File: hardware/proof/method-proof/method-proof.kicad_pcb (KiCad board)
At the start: 4 copper layers, 40 x 30 mm, 21 parts, among them J1 5V_IN, J2 OUT, J3 PA1, U1 MCP1700T-3302E/TT, U2 MSPS003F4SPW20R

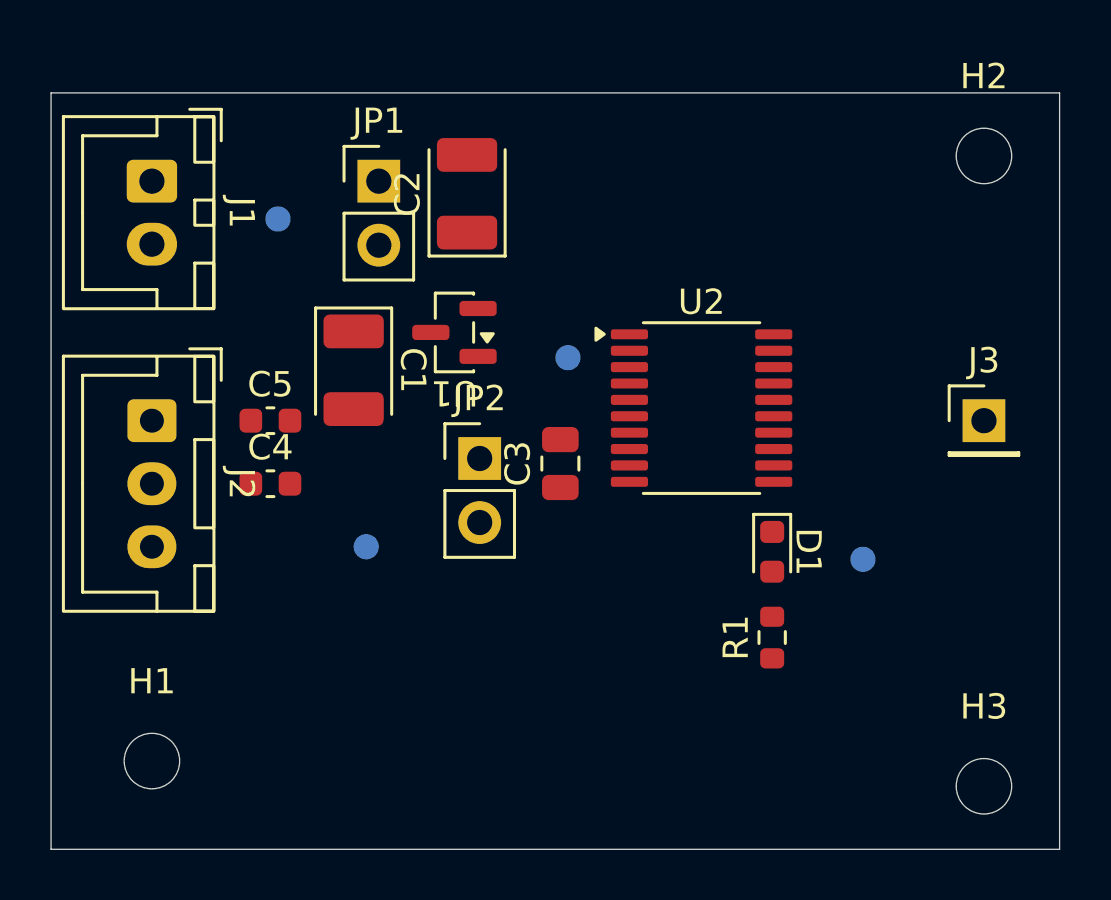
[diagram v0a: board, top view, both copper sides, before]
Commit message: hardware(method-proof): bring the footprints into step with their symbols and libraries: the symbols' fields, references on the fabrication layer, test points from the design's own library
Not for manufacture. Done with KiCad's scripting on the closed board, as the method
describes for what Konnect cannot do: each footprint carries its symbol's
description, datasheet and part fields, the mounting holes' BOM attribute follows
their symbols', the references move to the fabrication layers so no silkscreen
rule reaches them, and the four test points take the design's own footprint
library, whose copy Konnect can refresh from. The layout check reports no
violation but the unrouted connections.

Co-Authored-By: Claude Sonnet 5.5 <noreply@anthropic.com>
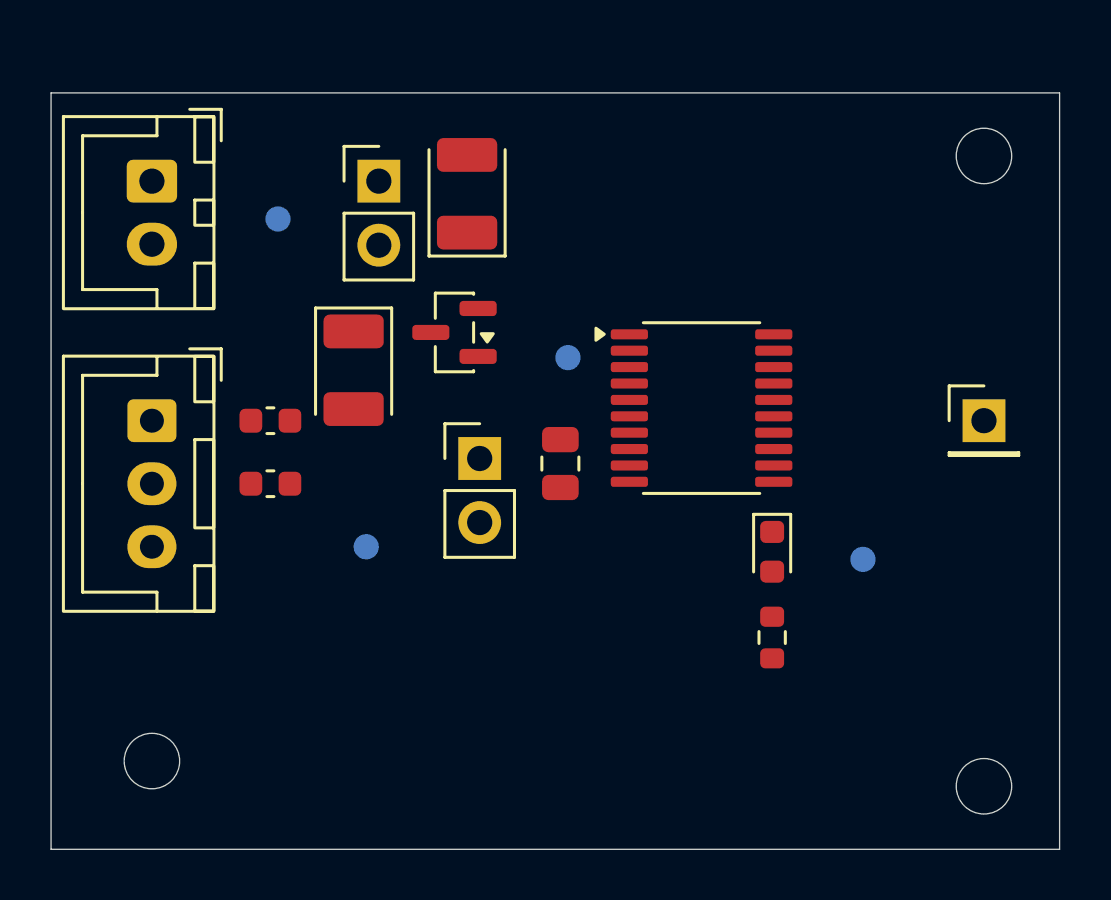
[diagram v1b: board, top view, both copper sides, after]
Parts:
- TP1, TP2, TP3, TP4: footprint TestPoint:TestPoint_Pad_D1.0mm -> method-proof:TestPoint_Pad_D1.0mm

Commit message: hardware(method-proof): critical nets routed by hand and locked: power, supply and ground tracks, vias, region pours and the GND planes on all four layers, DRC clean apart from the signal nets still to route
Co-Authored-By: Claude Sonnet 5.5 <noreply@anthropic.com>
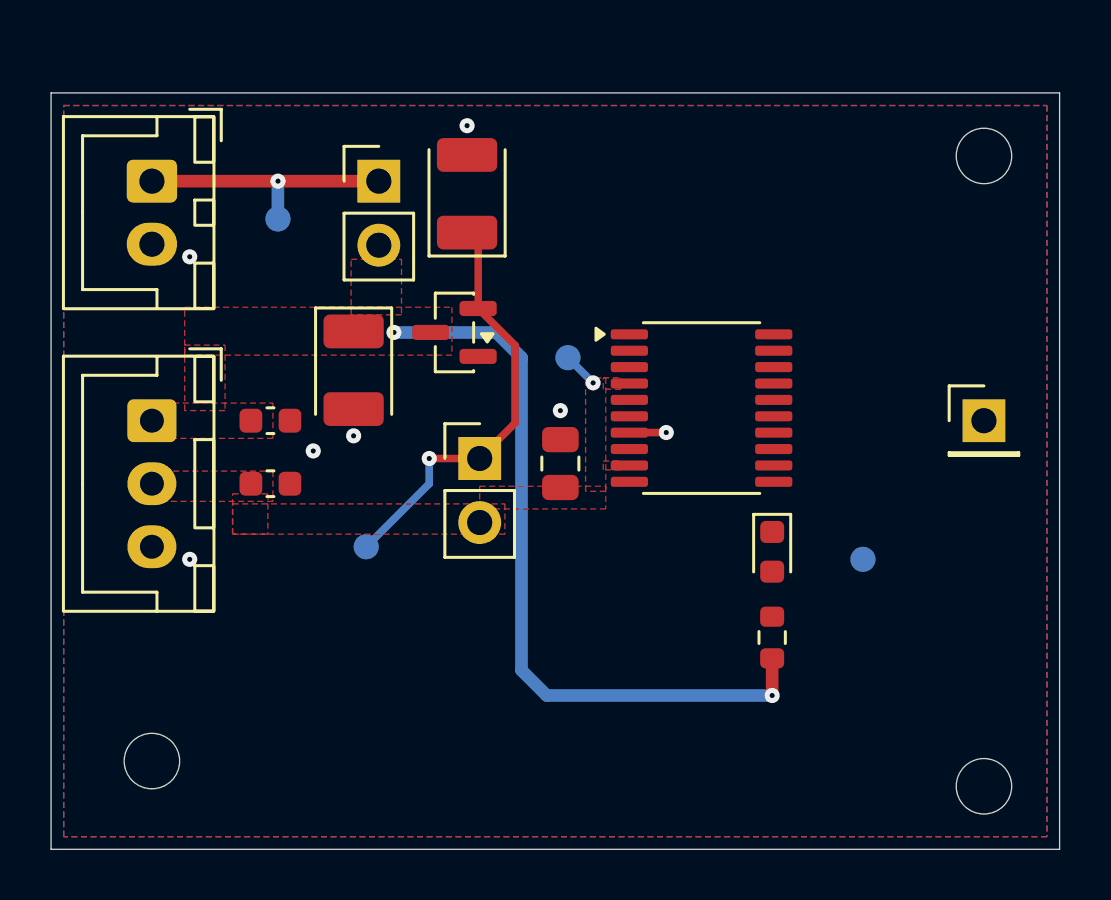
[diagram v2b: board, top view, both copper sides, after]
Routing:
- net +5V: track 0.00 -> 29.7 mm, vias 0 -> 2
- net /+3V3_REG: track 0.00 -> 16.7 mm, vias 0 -> 1
- net /+5V_IN: track 0.00 -> 10.5 mm, vias 0 -> 1
- net +3V3: track 0.00 -> 1.41 mm, vias 0 -> 1
- net GND: track 0.00 -> 1.10 mm, vias 0 -> 7
- added copper zone on F.Cu, net +3V3
- added copper zone on F.Cu, net +5V
- added copper zone on B.Cu, net GND
- added copper zone on F.Cu, net GND
- added copper zone on In1.Cu, net GND
- added copper zone on In2.Cu, net GND

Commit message: hardware(method-proof): three ground vias at each connector's return, one per 200 mA of the 0.5 A loop, relocked
Co-Authored-By: Claude Sonnet 5.5 <noreply@anthropic.com>
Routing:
- net GND: vias 7 -> 11
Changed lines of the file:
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@@
+	)
+	(via
+		(at 106.7 118.5)
+		(size 0.6)
+		(drill 0.2)
+		(layers "F.Cu" "B.Cu")
+		(locked yes)
+		(net "GND")
 	)
 	(via
@@
 	(via
 		(at 105.5 118.5)
+		(size 0.6)
+		(drill 0.2)
+		(layers "F.Cu" "B.Cu")
+		(locked yes)
+		(net "GND")
+	)
+	(via
+		(at 105.5 119.7)
 		(size 0.6)
 		(drill 0.2)
@@
 		(size 0.6)
 		(drill 0.2)
+		(layers "F.Cu" "B.Cu")
+		(locked yes)
+		(net "GND")
+	)
+	(via
+		(at 106.7 106.5)
+		(size 0.6)
+		(drill 0.2)
+		(layers "F.Cu" "B.Cu")
+		(locked yes)
+		(net "GND")
+	)
+	(via
+		(at 105.5 107.6)
+		(size 0.6)
+		(drill 0.2)
